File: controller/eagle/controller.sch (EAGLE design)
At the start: 9 parts, among them IC2 74HC04D, IC3 74HC590D, IC4 74HC151D, IC5 74HC151D, IC6 74HC151D, IC7 74HC151D, IC8 74HC08D

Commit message: controller board with eagle
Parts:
- removed IC2: 74HC04D, 74xx-eu:74HC04D
- removed IC3: 74HC590D, 74xx-eu:74HC590D
- removed IC4, IC5, IC6, IC7: 74HC151D, 74xx-eu:74HC151D
- removed IC8: 74HC08D, 74xx-eu:74HC08D
- removed JP1: (no value), pinhead:PINHD-1X3/90
- removed Q1: (no value), crystal:CRYSTAL68SMX
- added 8-BIT_COUNTER, 8-BIT_COUNTER1: 74HC590D, 74xx-eu:74HC590D
- added AND_01, AND_02: 74HC08D, 74xx-eu:74HC08D
- added C1: 100nF, rcl:C-EUC0805
- added C17, C20: 10pF, deto:C1
- added C9: 100nF, deto:C1
- added MUX_01, MUX_02, MUX_03, MUX_04, MUX_05, MUX_06, MUX_07, MUX_08: 74HC151D, 74xx-eu:74HC151D
- added NOT_01, NOT_02: 74HC04D, 74xx-eu:74HC04D
- added Q2: 4M9152, crystal:HC49UP
- added R12: Ferrit, deto:R2
- added R50: 1M, deto:R1
- added X1: KUSBVX-BS1N, con-kycon:KUSBVX-BS1N
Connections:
- new net +3.3V: 8-BIT_COUNTER1P.VCC, AND_02P.VCC, C1.1, MUX_05P.VCC, MUX_06P.VCC, MUX_07P.VCC, MUX_08P.VCC, NOT_02P.VCC
- new net AND_01A_OUT: AND_01A.O, MUX_04A.D3
- new net COUNTER_QA: 8-BIT_COUNTERA.QA, AND_01B.I1, MUX_01A.A, MUX_02A.A, MUX_03A.A
- new net COUNTER_QB: 8-BIT_COUNTERA.QB, AND_01B.I0, MUX_01A.B, MUX_02A.B, MUX_03A.B
- new net COUNTER_QC: 8-BIT_COUNTERA.QC, MUX_01A.C, MUX_02A.C, MUX_03A.C, NOT_01A.I
- new net COUNTER_QD: 8-BIT_COUNTERA.QD, MUX_04A.A
- new net COUNTER_QE: 8-BIT_COUNTERA.QE, MUX_04A.B
- new net EXTAL: 8-BIT_COUNTERA.CLK, C20.1, Q2.1, R50.1
- new net GND: 8-BIT_COUNTER1P.GND, AND_02P.GND, C1.2, C17.2, C20.2, C9.1, MUX_04A.C, MUX_05P.GND, MUX_06P.GND, MUX_07P.GND, MUX_08P.GND, NOT_02P.GND, X1.3, X1.4, X1.S1, X1.S2
- new net MUX_01_OUT: MUX_01A.Y, MUX_04A.D0
- new net MUX_02_OUT: MUX_02A.Y, MUX_04A.D1
- new net MUX_03_OUT: MUX_03A.Y, MUX_04A.D2
- new net N$1: R12.1, X1.1
- new net N$2: 8-BIT_COUNTERA.RCK, C17.1, Q2.2, R50.2
- new net N$3: AND_01B.O, NOT_01B.I
- new net N$4: AND_01A.I0, NOT_01A.O
- new net N$5: AND_01A.I1, NOT_01B.O
- new net SIGNAL_OUT: MUX_04A.Y, X1.2
- net +3V3: now also 8-BIT_COUNTERA.CCKEN, 8-BIT_COUNTERA.CCLR, 8-BIT_COUNTERA.RCO, C9.2, R12.2; no longer IC3A.CCKEN, IC3A.CCLR, IC3A.RCO

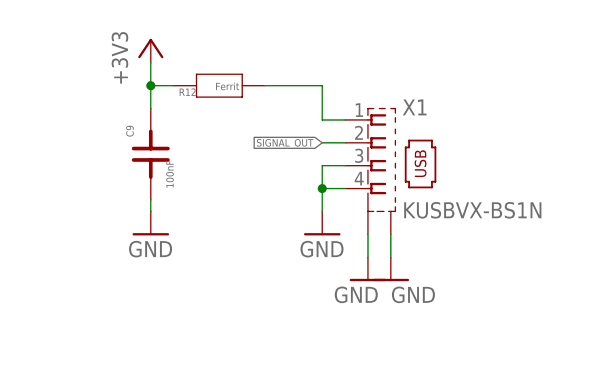
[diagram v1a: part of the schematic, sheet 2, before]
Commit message: usb type b
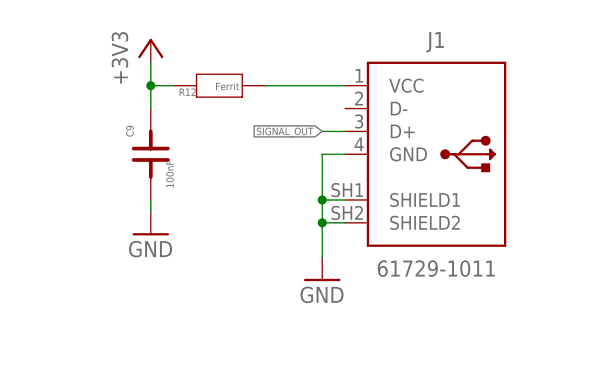
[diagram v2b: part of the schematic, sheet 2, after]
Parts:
- removed X1: KUSBVX-BS1N, con-kycon:KUSBVX-BS1N
- added J1: 61729-1011, Connector_USB:61729-1011
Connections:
- new net SHIELD1: J1.GND, J1.SHIELD1, J1.SHIELD2
- net GND: no longer X1.3, X1.4, X1.S1, X1.S2
- net N$1: now also J1.VCC; no longer X1.1
- net SIGNAL_OUT: now also J1.D+; no longer X1.2
